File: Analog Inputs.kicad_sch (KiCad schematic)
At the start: 28 parts, among them J10 Screw_Terminal_01x06, J8 Screw_Terminal_01x06, J9 Screw_Terminal_01x06, U3 REF35250QDBVR, U4 ADS1256, U5 ADS1256, Y1 8.0Mhz, Y2 8.0Mhz

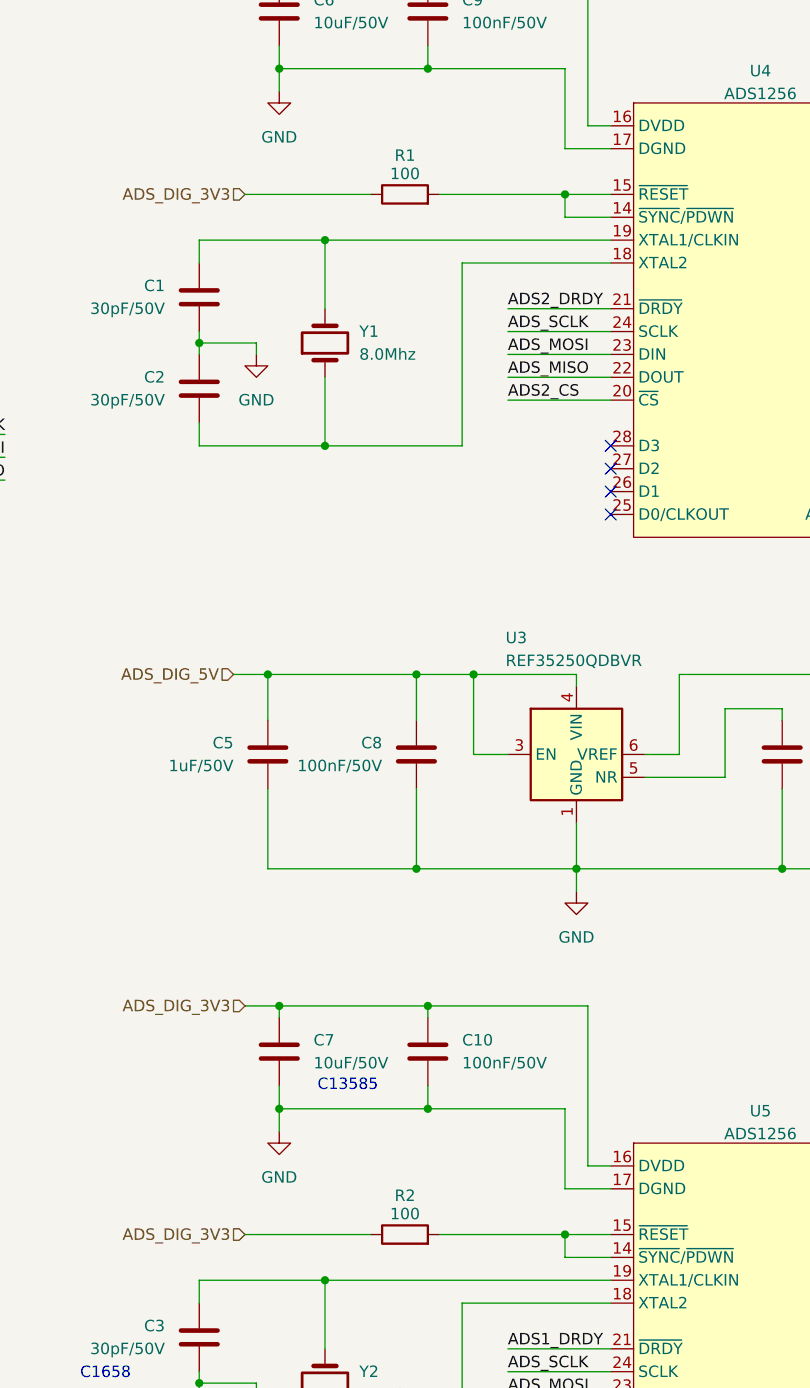
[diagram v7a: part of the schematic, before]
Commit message: Se añaden leds a la entrada de los Namur. Se estandariza y revisan varios footprints de los capacitores. El cambio no fue demasiado, se corrigio en placa. Se hacen algunos cambios adicionales a los valores. Se realiza un avance para jlcpcb
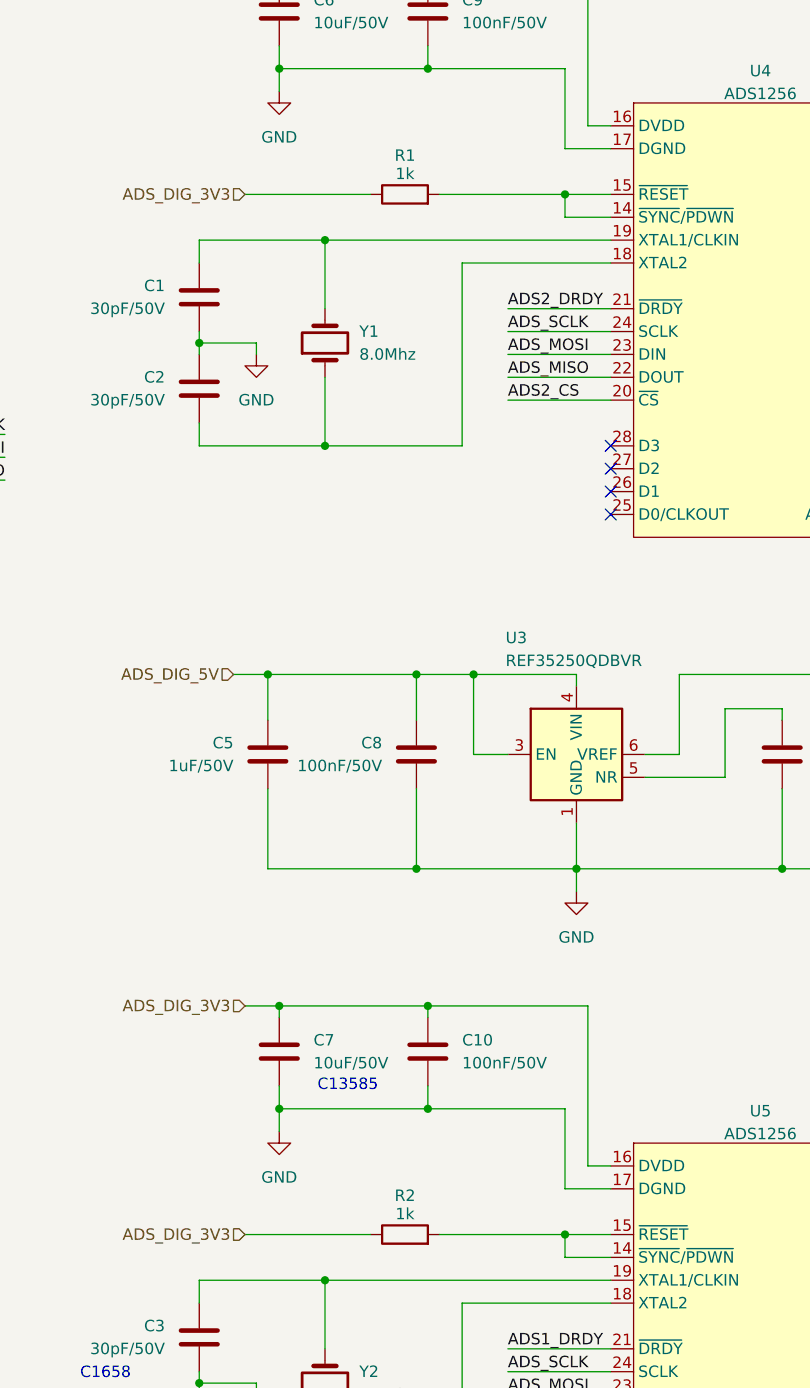
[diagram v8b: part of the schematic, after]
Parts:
- C10, C13, C14, C15, C16, C8, C9: footprint Resistor_SMD:R_0805_2012Metric_Pad1.20x1.40mm_HandSolder -> Capacitor_SMD:C_0603_1608Metric
- C11, C12, C5: footprint Resistor_SMD:R_0805_2012Metric_Pad1.20x1.40mm_HandSolder -> Capacitor_SMD:C_0805_2012Metric
- C17, C18, C6, C7: footprint Resistor_SMD:R_1206_3216Metric_Pad1.30x1.75mm_HandSolder -> Capacitor_SMD:C_1206_3216Metric
- R1, R2: value 100 -> 1k
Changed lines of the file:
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@@
 			)
 		)
-		(property "Footprint" "Resistor_SMD:R_0805_2012Metric_Pad1.20x1.40mm_HandSolder"
+		(property "Footprint" "Capacitor_SMD:C_0603_1608Metric"
 			(at 174.9552 205.74 0)
 			(effects
@@
 			)
 		)
-		(property "Footprint" "Resistor_SMD:R_0805_2012Metric_Pad1.20x1.40mm_HandSolder"
+		(property "Footprint" "Capacitor_SMD:C_0805_2012Metric"
 			(at 166.0652 151.13 0)
 			(effects
@@
 			)
 		)
-		(property "Footprint" "Resistor_SMD:R_1206_3216Metric_Pad1.30x1.75mm_HandSolder"
+		(property "Footprint" "Capacitor_SMD:C_1206_3216Metric"
 			(at 92.4052 184.15 0)
 			(effects
@@
 			)
 		)
-		(property "Footprint" "Resistor_SMD:R_1206_3216Metric_Pad1.30x1.75mm_HandSolder"
+		(property "Footprint" "Capacitor_SMD:C_1206_3216Metric"
 			(at 192.7352 68.58 0)
 			(effects
@@
 			)
 		)
-		(property "Value" "100"
+		(property "Value" "1k"
 			(at 105.41 198.374 90)
 			(effects
@@
 			)
 		)
-		(property "Footprint" "Resistor_SMD:R_0805_2012Metric_Pad1.20x1.40mm_HandSolder"
+		(property "Footprint" "Capacitor_SMD:C_0603_1608Metric"
 			(at 174.9552 68.58 0)
 			(effects
@@
 			)
 		)
-		(property "Footprint" "Resistor_SMD:R_1206_3216Metric_Pad1.30x1.75mm_HandSolder"
+		(property "Footprint" "Capacitor_SMD:C_1206_3216Metric"
 			(at 192.7352 184.15 0)
 			(effects
@@
 			)
 		)
-		(property "Footprint" "Resistor_SMD:R_0805_2012Metric_Pad1.20x1.40mm_HandSolder"
+		(property "Footprint" "Capacitor_SMD:C_0603_1608Metric"
 			(at 105.7148 151.13 0)
 			(effects
@@
 			)
 		)
-		(property "Value" "100"
+		(property "Value" "1k"
 			(at 105.41 82.804 90)
 			(effects
@@
 			)
 		)
-		(property "Footprint" "Resistor_SMD:R_0805_2012Metric_Pad1.20x1.40mm_HandSolder"
+		(property "Footprint" "Capacitor_SMD:C_0603_1608Metric"
 			(at 174.9552 90.17 0)
 			(effects
@@
 			)
 		)
-		(property "Footprint" "Resistor_SMD:R_0805_2012Metric_Pad1.20x1.40mm_HandSolder"
+		(property "Footprint" "Capacitor_SMD:C_0603_1608Metric"
 			(at 174.9552 184.15 0)
 			(effects
@@
 			)
 		)
-		(property "Footprint" "Resistor_SMD:R_0805_2012Metric_Pad1.20x1.40mm_HandSolder"
+		(property "Footprint" "Capacitor_SMD:C_0805_2012Metric"
 			(at 148.2852 151.13 0)
 			(effects
@@
 			)
 		)
-		(property "Footprint" "Resistor_SMD:R_0805_2012Metric_Pad1.20x1.40mm_HandSolder"
+		(property "Footprint" "Capacitor_SMD:C_0603_1608Metric"
 			(at 108.9152 184.15 0)
 			(effects
@@
 			)
 		)
-		(property "Footprint" "Resistor_SMD:R_1206_3216Metric_Pad1.30x1.75mm_HandSolder"
+		(property "Footprint" "Capacitor_SMD:C_1206_3216Metric"
 			(at 92.4052 68.58 0)
 			(effects
@@
 			)
 		)
-		(property "Footprint" "Resistor_SMD:R_0805_2012Metric_Pad1.20x1.40mm_HandSolder"
+		(property "Footprint" "Capacitor_SMD:C_0603_1608Metric"
 			(at 108.9152 68.58 0)
 			(effects
@@
 			)
 		)
-		(property "Footprint" "Resistor_SMD:R_0805_2012Metric_Pad1.20x1.40mm_HandSolder"
+		(property "Footprint" "Capacitor_SMD:C_0805_2012Metric"
 			(at 91.1352 151.13 0)
 			(effects
